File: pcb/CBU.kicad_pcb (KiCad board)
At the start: 2 copper layers, 43.8 x 31.8 mm, 54 parts, among them J1 Conn_01x03_Socket, J11 Conn_01x03_Pin, J4 Conn_01x02_Socket, J5 Conn_01x02_Socket, J6 Conn_01x03_Socket, J7 Conn_01x03_Socket, J9 USB_C_Receptacle, Q1 AO3416A, Q2 AO3416A, Q3 AO3416A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

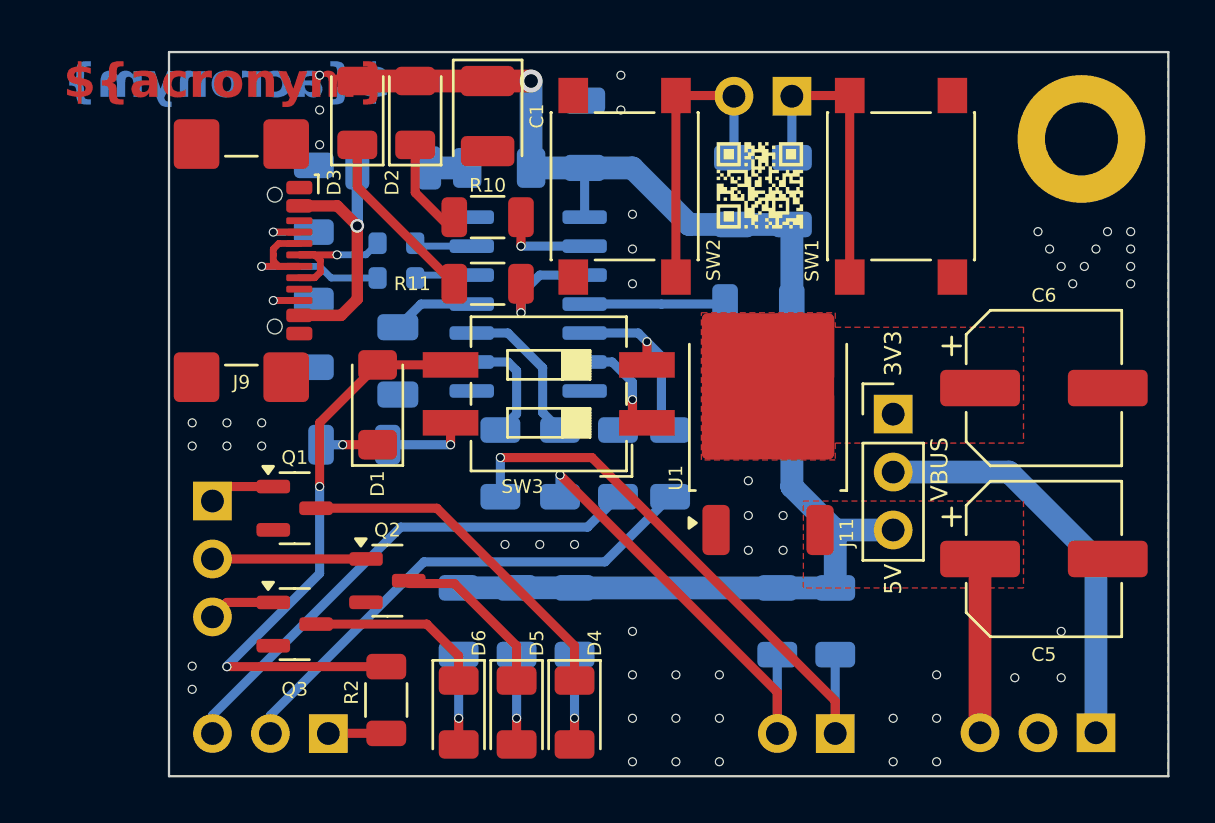
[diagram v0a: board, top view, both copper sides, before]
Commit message: Change MCP2221A to FT230X
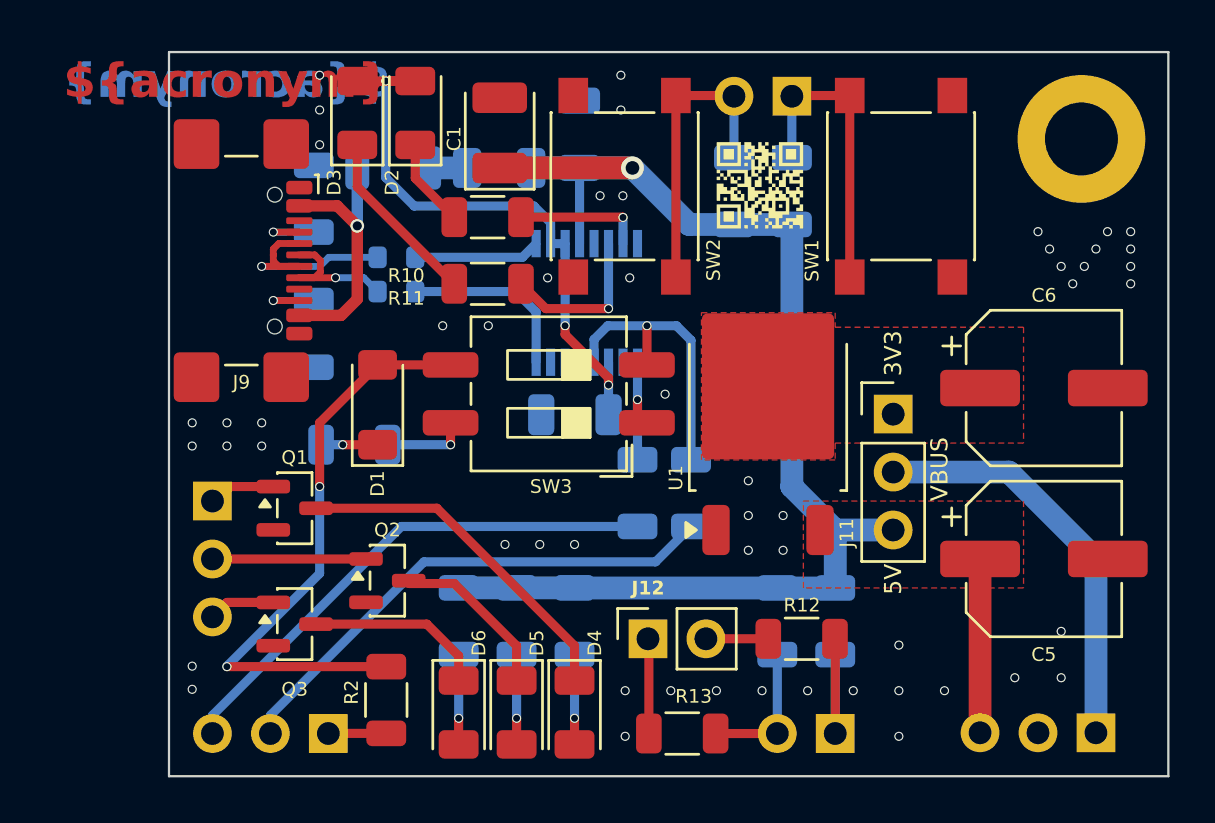
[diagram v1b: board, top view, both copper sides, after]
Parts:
- removed C4: 10n, Capacitor_SMD:C_1206_3216Metric
- removed R3: 1k, Resistor_SMD:R_1206_3216Metric
- added J12: Conn_01x02_Socket, Connector_PinSocket_2.54mm:PinSocket_1x02_P2.54mm_Vertical, F.Cu at (148.3, 101.9)
- R12, R13: moved to F.Cu
- U2: value MCP2221AxSL -> FT230XS; footprint Package_SO:SOIC-14_3.9x8.7mm_P1.27mm -> Package_SO:SSOP-16_3.9x4.9mm_P0.635mm
- moved R12 15.3 mm to (155.0, 101.9), turned to 180 degrees
- moved R13 13.0 mm to (149.8, 106.0), turned to 180 degrees
- moved C3 8.11 mm to (145.1, 92.1), turned to 180 degrees
- moved U2 2.57 mm to (145.6, 87.2), turned to 90 degrees
- moved R7 2.12 mm to (137.2, 86.7)
- moved R6 1.59 mm to (150.1, 95.5)
- moved R8 1.56 mm to (147.8, 95.5)
- moved C1 0.91 mm to (141.8, 79.7), turned to 90 degrees
- moved R9 0.91 mm to (137.2, 85.2)
- moved C2 0.22 mm to (145.3, 79.8)
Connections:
- C3 pad 1: Net-(U2-VUSB) -> Net-(D2-A)
- D2 pad 2: +5V -> Net-(D2-A)
- D3 pad 2: +5V -> Net-(D2-A)
- R10 pad 2: Net-(U2-GP0) -> Net-(U2-CBUS0)
- R11 pad 2: Net-(U2-GP1) -> Net-(U2-CBUS1)
- R12 pad 2: Net-(U2-SDA) -> Net-(J12-Pin_2)
- R13 pad 2: Net-(U2-SCL) -> Net-(J12-Pin_1)
- R6 pad 2: Net-(U2-URx) -> Net-(U2-RXD)
- R7 pad 2: Net-(U2-D+) -> Net-(U2-USBDP)
- R8 pad 2: Net-(U2-UTx) -> Net-(U2-TXD)
- R9 pad 2: Net-(U2-D-) -> Net-(U2-USBDM)
- SW3 pad 1: Net-(U2-UTx) -> Net-(U2-TXD)
- SW3 pad 2: Net-(U2-URx) -> Net-(U2-RXD)
- U2 pad 1: +5V -> Net-(U2-TXD)
- U2 pad 10: Net-(U2-SCL) -> Net-(D2-A)
- U2 pad 11: Net-(U2-VUSB) -> Net-(D2-A)
- U2 pad 12: Net-(U2-D-) -> +5V
- U2 pad 13: Net-(U2-D+) -> GND
- U2 pad 14: GND -> Net-(U2-CBUS1)
- U2 pad 2: Net-(U2-GP0) -> unconnected-(U2-~{RTS}-Pad2)
- U2 pad 3: Net-(U2-GP1) -> Net-(D2-A)
- U2 pad 4: Net-(U2-~{RST}) -> Net-(U2-RXD)
- U2 pad 5: Net-(U2-URx) -> GND
- U2 pad 6: Net-(U2-UTx) -> unconnected-(U2-~{CTS}-Pad6)
- U2 pad 8: unconnected-(U2-GP3-Pad8) -> Net-(U2-USBDP)
- U2 pad 9: Net-(U2-SDA) -> Net-(U2-USBDM)
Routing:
- net Net-(D2-A): track 0.00 -> 26.9 mm, vias 0 -> 3
- net /SDA: track 25.7 -> 7.61 mm, vias 1 -> 0
- net /SCL: track 19.7 -> 6.16 mm, vias 1 -> 0
- net Net-(U2-RXD): track 0.00 -> 12.7 mm, vias 0 -> 1
- net Net-(U2-~{RST}): track 8.32 -> 0.00 mm
- net Net-(U2-URx): track 8.20 -> 0.00 mm, vias 1 -> 0
- net Net-(U2-USBDP): track 0.00 -> 7.88 mm
- net Net-(U2-CBUS1): track 0.00 -> 7.14 mm, vias 0 -> 1
- net Net-(U2-SCL): track 6.79 -> 0.00 mm
- net Net-(U2-UTx): track 6.47 -> 0.00 mm, vias 1 -> 0
- net Net-(U2-CBUS0): track 0.00 -> 5.63 mm, vias 0 -> 1
- net Net-(U2-USBDM): track 0.00 -> 5.55 mm
- net Net-(U2-TXD): track 0.00 -> 5.46 mm, vias 0 -> 1
- net Net-(U2-GP1): track 5.23 -> 0.00 mm, vias 1 -> 0
- net Net-(U2-SDA): track 5.02 -> 0.00 mm
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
